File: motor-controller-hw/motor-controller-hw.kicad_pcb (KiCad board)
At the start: 4 copper layers, 162 parts, among them J101 CAN, J102 Throttle, J103 Motor Temp, J104 Transistor Temp, J105 USB_B_Micro, J106 Extra IO, J107 Hall Sensors, J108 CAN_DBG, J109 ABN Encoder, J110 SPI_DBG, J111 Trinamic-Bridge, J301 SWD, J302 User USART, J401 Trinamic_TRMI, J402 TMC4671 USART, Q101 Q_PMOS_GDS, SW301 Reset, SW302 Boot, SW303 User_SW, U101 AP7361C-33, U102 D36V6F5, U201 MCP6004, U202 MCP6004, U203 MCP6004, U204 74HC7014, U205 74HC7014, U206 mcp2562, U301 STM32F303RETx, U401 TMC4671, X401 IQXO-50, Y301 8Mhz

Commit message: Moved chaged order of op-amps to make PCB layout easier. More pcb part positioning
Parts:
- C101, C102, C104, C105, C202, C203, C204, C205, C301, C302, C303, C304, C305, C306, C307, C308, C309, C310, C311, C401, C403, C404, C406, C408, C409, C410, C411, R201, R202, R203, R206, R207, R208, R209, R213, R214, R215, R301, R303, R304, U201, U202: moved to B.Cu
- TP401, TP402: footprint Connector_PinHeader_2.54mm:PinHeader_1x03_P2.54mm_Vertical -> Pin_Headers:Pin_Header_Straight_1x01_Pitch2.54mm
- moved C420 307.0 mm to (88.3, 59.9), turned to 270 degrees
- moved R409 307.0 mm to (88.3, 56.1), turned to 90 degrees
- moved C402 305.8 mm to (87.6, 41.3), turned to 270 degrees
- moved R408 303.4 mm to (87.2, 69.1), turned to 270 degrees
- moved R401 302.8 mm to (87.6, 37.5), turned to 270 degrees
- moved R403 301.9 mm to (92.3, 37.3), turned to 270 degrees
- moved C419 301.2 mm to (89.3, 69.1), turned to 270 degrees
- moved R402 298.0 mm to (85.6, 41.3), turned to 270 degrees
- moved R404 296.8 mm to (92.3, 41.1), turned to 270 degrees
- moved R410 293.8 mm to (89.3, 65.3), turned to 270 degrees
- moved C407 293.5 mm to (90.3, 41.1), turned to 270 degrees
- moved R406 293.3 mm to (95.0, 56.1), turned to 270 degrees
- moved C417 292.6 mm to (95.0, 59.9), turned to 270 degrees
- moved C418 289.4 mm to (100.8, 60.1), turned to 270 degrees
- moved R407 283.8 mm to (100.8, 56.1), turned to 270 degrees
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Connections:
- J110 pad 3: /TMC4671/SPI_MOSI -> /TMC4671/SPI_MISO
- J110 pad 4: /TMC4671/SPI_MISO -> /TMC4671/SPI_MOSI
- U201 pad 1: Net-(R201-Pad2) -> /A_Out2
- U201 pad 10: /IO Protection/A_Out1 -> /Throttle
- U201 pad 12: /IO Protection/A_Out2 -> Net-(C203-Pad1)
- U201 pad 13: /A_Out2 -> /IO Protection/Throttle
- U201 pad 14: /A_Out2 -> /IO Protection/Throttle
- U201 pad 2: Net-(R201-Pad2) -> /A_Out2
- U201 pad 3: /Throttle -> /IO Protection/A_Out2
- U201 pad 5: Net-(C203-Pad1) -> /IO Protection/A_Out1
- U201 pad 6: /IO Protection/Throttle -> /A_Out1
- U201 pad 7: /IO Protection/Throttle -> /A_Out1
- U201 pad 8: /A_Out1 -> Net-(R201-Pad2)
- U201 pad 9: /A_Out1 -> Net-(R201-Pad2)

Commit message: Working PCB Layout
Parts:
- C212, C215, C216, C217, C218, C219, C220, D101, R102, R210, R211, R212, R216, R217, R218, R219, R220, R408, U205: moved to B.Cu
- R207, R208, R209, R213, R214, R215: moved to F.Cu
- moved R408 179.0 mm to (265.9, 57.9), turned to 0 degrees
- moved R409 178.1 mm to (265.9, 68.1), turned to 180 degrees
- moved C420 177.8 mm to (265.9, 66.0), turned to 0 degrees
- moved C419 177.0 mm to (265.9, 57.9), turned to 0 degrees
- moved R410 176.7 mm to (265.9, 59.9), turned to 180 degrees
- moved R406 171.1 mm to (265.9, 64.0), turned to 180 degrees
- moved C417 171.0 mm to (265.9, 62.0), turned to 0 degrees
- moved R407 165.9 mm to (265.9, 72.1), turned to 180 degrees
- moved C418 165.4 mm to (265.9, 70.1), turned to 0 degrees
- moved R403 161.2 mm to (249.8, 71.6)
- moved R404 161.2 mm to (249.8, 75.4)
- moved C407 161.2 mm to (247.8, 75.4)
- moved C402 160.1 mm to (244.0, 75.5)
- moved R401 160.1 mm to (244.0, 71.7)
- moved R402 160.1 mm to (242.0, 75.5)
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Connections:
- C420 pad 1: /Batt_Current -> /TMC4671/Batt_I
- D301 pad 1: Net-(D301-Pad1) -> GNDD
- D301 pad 2: /STM32/CAN_Status -> Net-(D301-Pad2)
- D302 pad 1: Net-(D302-Pad1) -> GNDD
- D302 pad 2: /STM32/Heartbeat -> Net-(D302-Pad2)
- D303 pad 1: Net-(D303-Pad1) -> GNDD
- D303 pad 2: /STM32/User_LED -> Net-(D303-Pad2)
- R305 pad 1: GNDD -> Net-(D301-Pad2)
- R305 pad 2: Net-(D301-Pad1) -> /STM32/CAN_Status
- R306 pad 1: GNDD -> Net-(D302-Pad2)
- R306 pad 2: Net-(D302-Pad1) -> /STM32/Heartbeat
- R307 pad 1: GNDD -> Net-(D303-Pad2)
- R307 pad 2: Net-(D303-Pad1) -> /STM32/User_LED
- R409 pad 2: /Batt_Current -> /TMC4671/Batt_I
- TP422 pad 2: /Batt_Current -> /TMC4671/Batt_I
- U401 pad 21: /Batt_Current -> /TMC4671/Batt_I

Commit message: Started routing
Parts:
- moved J402 0.19 mm to (227.3, 68.3)
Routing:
- net GNDD: track 0.00 -> 6.33 mm, vias 0 -> 1
- net /Throttle: track 0.00 -> 6.32 mm, vias 0 -> 1
- net Net-(R202-Pad2): track 0.00 -> 5.65 mm
- net Net-(C203-Pad1): track 0.00 -> 4.48 mm
- net Net-(C205-Pad1): track 0.00 -> 4.29 mm
- net Net-(C204-Pad1): track 0.00 -> 4.13 mm
- net Net-(R201-Pad2): track 0.00 -> 3.80 mm
- net Net-(R203-Pad2): track 0.00 -> 3.68 mm
- net /IO Protection/Throttle: track 0.00 -> 1.27 mm
- net /A_Out1: track 0.00 -> 1.27 mm
- net /A_Out2: track 0.00 -> 1.27 mm
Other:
- net class Default: clearance 0.2 -> 0.1778; trace_width 0.25 -> 0.3048; via_dia 0.8 -> 0.762; via_drill 0.4 -> 0.381
- net class analog_signal added: clearance 0.1778, trace_width 0.3048, via_dia 0.762, via_drill 0.381
- net class power added: clearance 0.254, trace_width 0.508, via_dia 1.4224, via_drill 1.016
- net class serial_signal added: clearance 0.1778, trace_width 0.2032, via_dia 0.762, via_drill 0.381
- net class small_signal added: clearance 0.1778, trace_width 0.2032, via_dia 0.762, via_drill 0.381
- rule trace_clearance: 0.2 -> 0.1778
- rule trace_min: 0.2 -> 0.1524
- rule via_min_drill: 0.3 -> 0.254
- rule via_min_size: 0.4 -> 0.508

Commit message: PCB Routing
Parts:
- moved C213 159.2 mm to (31.4, 69.7)
- moved C214 159.2 mm to (31.3, 66.2)
- moved C415 159.2 mm to (33.5, 60.3)
- moved C416 159.2 mm to (30.1, 60.1)
- moved C210 148.1 mm to (100.3, 113.0), turned to 90 degrees
- moved C216 147.5 mm to (111.1, 121.3)
- moved C219 147.5 mm to (94.9, 121.6)
- moved C402 147.5 mm to (101.4, 113.0)
- moved J109 147.5 mm to (99.3, 129.6)
- moved R208 147.5 mm to (111.1, 121.3)
- moved R211 147.5 mm to (111.1, 116.7)
- moved R214 147.5 mm to (94.9, 121.6)
- moved R218 147.5 mm to (94.9, 117.0)
- moved R401 147.5 mm to (101.4, 109.2)
- moved C215 147.5 mm to (109.1, 121.3)
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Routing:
- net +5V: track 0.00 -> 322.6 mm, vias 0 -> 12
- net GNDD: track 6.33 -> 285.8 mm, vias 1 -> 45
- net +3V3: track 0.00 -> 99.8 mm, vias 0 -> 27
- net /MotorTemp: track 0.00 -> 95.7 mm, vias 0 -> 1
- net +BATT: track 0.00 -> 78.8 mm, vias 0 -> 2
- net /SPI_SS: track 0.00 -> 77.5 mm, vias 0 -> 2
- net /Vin: track 0.00 -> 73.3 mm, vias 0 -> 1
- net /SPI_MISO: track 0.00 -> 70.5 mm, vias 0 -> 2
- net /TMC4671/1v8: track 0.00 -> 70.3 mm, vias 0 -> 8
- net /SPI_MOSI: track 0.00 -> 68.3 mm, vias 0 -> 2
- net /SPI_SCK: track 0.00 -> 64.4 mm, vias 0 -> 2
- net /A_Out1: track 1.27 -> 61.8 mm, vias 0 -> 1
- net /A_Out2: track 1.27 -> 58.8 mm, vias 0 -> 1
- net /TMC4671/En_In: track 0.00 -> 47.9 mm, vias 0 -> 2
- net /TMC4671/B_Current: track 0.00 -> 42.5 mm, vias 0 -> 1
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- added copper zone on In2.Cu, net +3V3
- added copper zone on In1.Cu, net GNDD
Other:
- net class serial_signal: trace_width 0.2032 -> 0.254

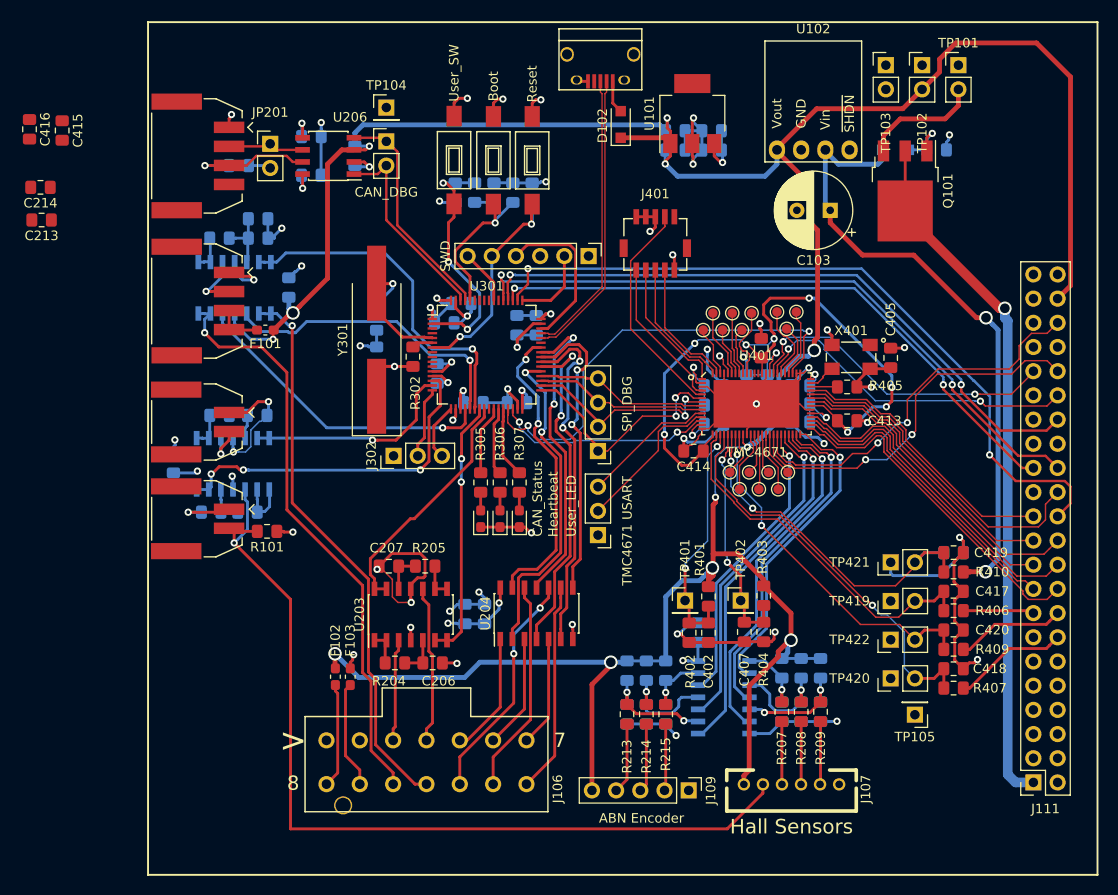
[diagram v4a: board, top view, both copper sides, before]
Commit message: Added mounting holes to pcb
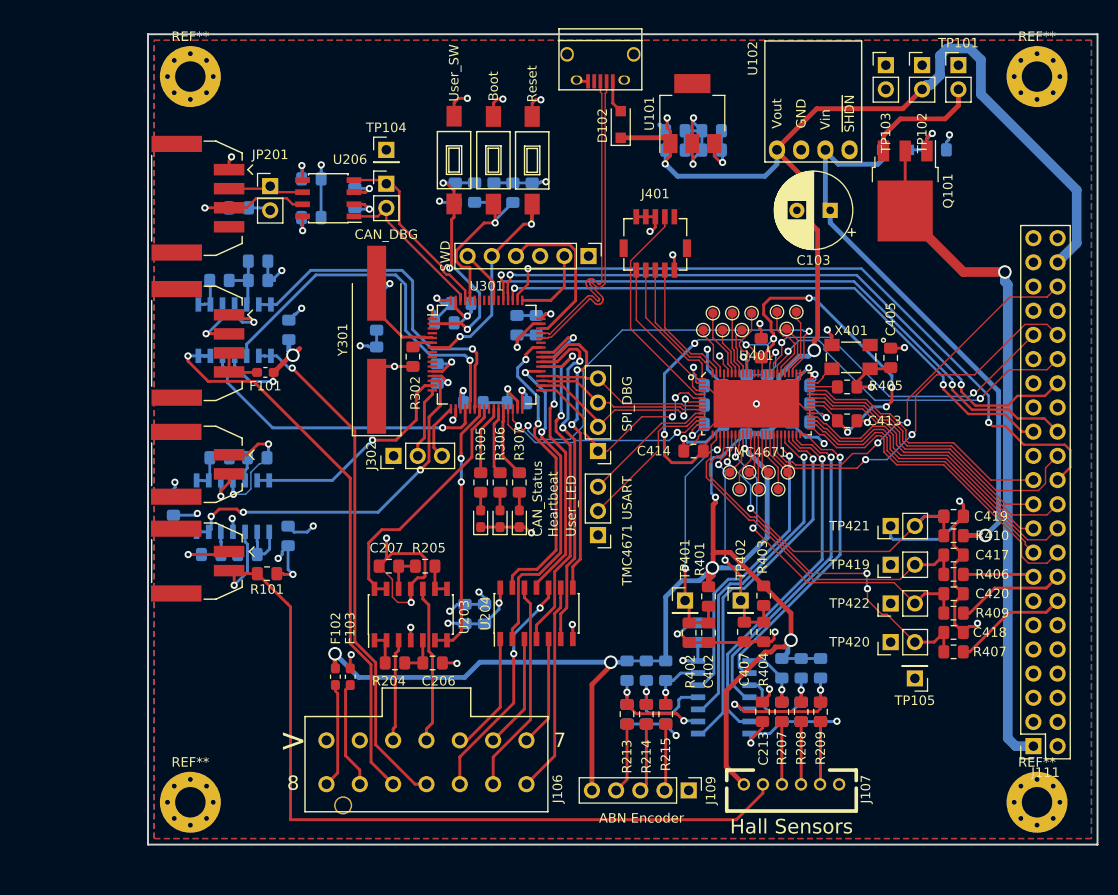
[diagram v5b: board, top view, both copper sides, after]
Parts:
- added REF**: MountingHole_3.2mm_M3_Pad_Via, Mounting_Holes:MountingHole_3.2mm_M3_Pad_Via, F.Cu at (135.9, 130.8)
- added REF**: MountingHole_3.2mm_M3_Pad_Via, Mounting_Holes:MountingHole_3.2mm_M3_Pad_Via, F.Cu at (47.0, 54.6)
- added REF**: MountingHole_3.2mm_M3_Pad_Via, Mounting_Holes:MountingHole_3.2mm_M3_Pad_Via, F.Cu at (47.0, 130.8)
- added REF**: MountingHole_3.2mm_M3_Pad_Via, Mounting_Holes:MountingHole_3.2mm_M3_Pad_Via, F.Cu at (135.9, 54.6)
- C214, C415, C416: moved to B.Cu
- moved C213 91.6 mm to (107.1, 121.3), turned to 270 degrees
- moved C416 83.4 mm to (107.5, 91.1), turned to 90 degrees
- moved C415 78.1 mm to (105.3, 91.1), turned to 90 degrees
- moved C214 44.9 mm to (57.3, 102.8), turned to 90 degrees
- moved C201 4.45 mm to (57.3, 81.2)
- moved C203 4.45 mm to (54.1, 74.0)
- moved C204 4.45 mm to (49.2, 104.8)
- moved C212 4.45 mm to (59.7, 65.4)
- moved JP201 4.45 mm to (55.4, 66.1)
- moved R101 4.45 mm to (55.0, 106.8)
- moved R202 4.45 mm to (53.0, 104.8)
- moved U201 4.45 mm to (51.6, 81.2)
- moved U202 4.45 mm to (51.5, 99.7)
- moved C202 4.45 mm to (64.3, 67.4)
- moved J101 4.45 mm to (42.9, 67.4)
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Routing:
- net GNDD: track 285.8 -> 351.4 mm, vias 45 -> 47
- net +5V: track 322.6 -> 283.2 mm
- net +BATT: track 78.8 -> 71.3 mm, vias 2 -> 1
- net /IO Protection/A_Out2: track 31.9 -> 39.4 mm
- net +3V3: track 99.8 -> 106.4 mm, vias 27 -> 29
- net /MotorTemp: track 95.7 -> 90.1 mm
- net /A_Out2: track 58.8 -> 54.3 mm
- net /IO Protection/CAN_Rx: track 23.7 -> 19.8 mm
- net Net-(C217-Pad1): track 11.8 -> 15.7 mm
- net /IO Protection/CAN_Tx: track 21.1 -> 17.3 mm
- net /USB_D-: track 30.7 -> 34.3 mm
- net /SPI_SS: track 77.5 -> 74.0 mm
- net /USB_D+: track 30.2 -> 33.7 mm
- net /IO Protection/TransistorTemp: track 22.4 -> 24.4 mm
- net /IO Protection/MotorTemp: track 36.4 -> 38.3 mm
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- added copper zone on B.Cu, net +5V
- added copper zone on F.Cu, net +5V
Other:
- board outline added: 99.7 x 85.1 mm
- net class power: clearance 0.254 -> 0.1778
- rule trace_min: 0.1524 -> 0.127

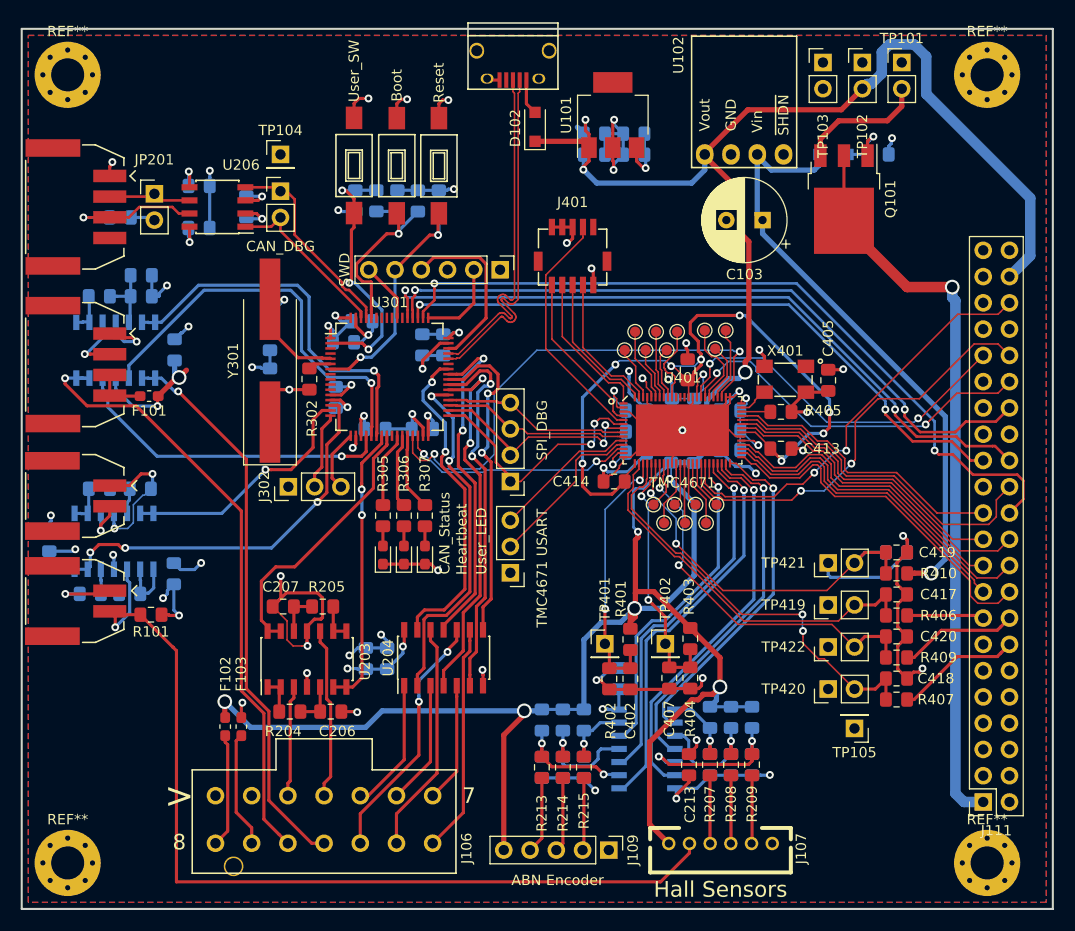
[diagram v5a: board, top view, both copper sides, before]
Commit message: Adding BOM, changed some footprints -Changed footprints to linux models in schematics -Added field Digi-key# to all components -Started filling in said field
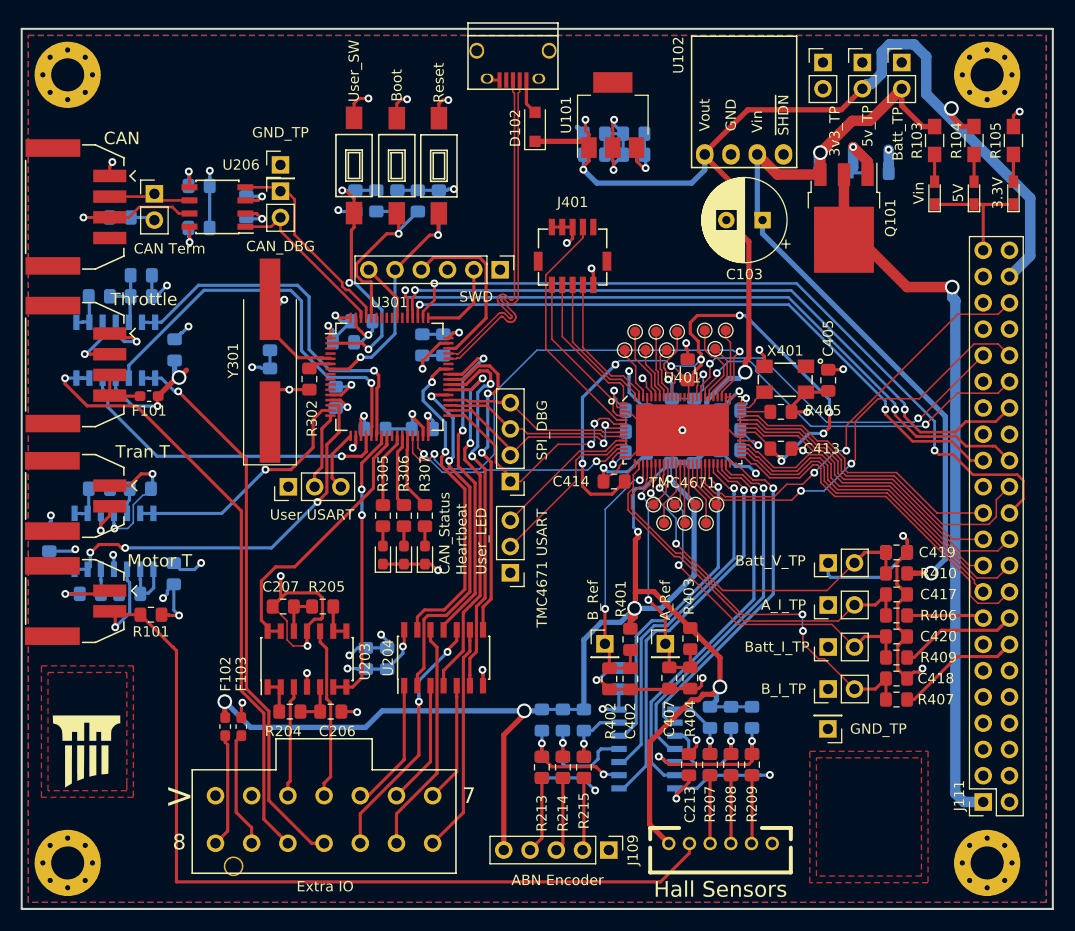
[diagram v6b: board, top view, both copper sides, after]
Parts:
- added D103: Vin, LEDs:LED_0603_HandSoldering, F.Cu at (130.8, 66.0)
- added D104: 5V, LEDs:LED_0603_HandSoldering, F.Cu at (134.6, 66.0)
- added D105: 3.3V, LEDs:LED_0603_HandSoldering, F.Cu at (138.4, 66.0)
- added G***: LOGO, supermileage_footprints:cedarville-logo, F.Cu at (49.0, 118.6)
- added G***: LOGO, supermileage_footprints:shell-logo, F.Cu at (24.6, 145.8)
- added G***: LOGO, supermileage_footprints:shell-logo, F.Cu at (124.5, 126.4)
- added R103: 10K, Resistors_SMD:R_0805_HandSoldering, F.Cu at (130.8, 61.0)
- added R104: 1K, Resistors_SMD:R_0805_HandSoldering, F.Cu at (134.6, 61.0)
- added R105: 510R, Resistors_SMD:R_0805_HandSoldering, F.Cu at (138.4, 61.0)
- C215, C216, C217, C218, C219, C220: value 100n -> 100p
- C417, C418, C420: value 100n -> 10n
- J103: value Motor Temp -> Motor T
- J104: value Transistor Temp -> Tran T
- JP201: value CAN Termination -> CAN Term
- TP101: value 5v_TP -> Batt_TP
- moved TP105 2.57 mm to (120.5, 117.9)
- moved Q101 1.83 mm to (122.0, 68.5)
- moved D101 1.78 mm to (121.0, 64.1)
- moved R102 1.78 mm to (125.3, 64.1)
- moved TP104 1.02 mm to (67.6, 63.3)
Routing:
- net GNDD: track 351.4 -> 364.8 mm
- net +BATT: track 71.3 -> 78.0 mm, vias 1 -> 2
- net +5V: track 283.2 -> 287.7 mm, vias 12 -> 13
- net Net-(D105-Pad2): track 0.00 -> 2.63 mm
- net Net-(D104-Pad2): track 0.00 -> 2.63 mm
- net Net-(D103-Pad2): track 0.00 -> 2.63 mm
- net +3V3: track 106.4 -> 108.2 mm, vias 29 -> 30
- net Net-(D101-Pad2): track 6.01 -> 7.83 mm
- added copper zone on F.Cu, net (none)
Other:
- board text added: "CAN 1. >GND 2. CANL 3. CANH 4. N/C"
- board text added: "Cedarville University Samuel Ellicott: Fall 2018"
- board text added: "Extra IO 1. GND | 8. 5v 2. GND | 9. 3.3v 3. Ain1 | 10. Aout1 4. Ain2 | 11. Aout 2 5. Din1 | 12. Dout 1 6. Din2 | 13. Dout 2 7. Din3 | 14. Din 4"
- board text added: "High Efficiency Motor Controller Control PCB - v1.0"
- board text added: "Motor Temp 1. >GND 2. Temp in"
- board text added: "Throttle 1. >GND 2. Throttle 3. 5v 4. 5v"
- board text added: "Transistor Temp 1. >GND 2. Temp in"

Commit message: Moved some parts into the project parts library messed with the PCB slightly
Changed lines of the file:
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@@
-(kicad_pcb (version 20171130) (host pcbnew "(5.0.0-rc2-dev-670-ga3770bf6e)")
+(kicad_pcb (version 20171130) (host pcbnew 5.0.1)
   (general
     (thickness 1.6)
@@
     (pad_drill 3.2)
     (pad_to_mask_clearance 0.2)
+    (solder_mask_min_width 0.25)
     (aux_axis_origin 0 0)
     (visible_elements 7FFFFF7F)
@@
       (hpglpennumber 1)
       (hpglpenspeed 20)
-      (hpglpendiameter 15)
+      (hpglpendiameter 15.000000)
       (psnegative false)
       (psa4output false)
@@
     (tags "capacitor handsolder")
     (attr smd)
-    (fp_text reference C401 (at -3.8862 0.635 270) (layer B.SilkS)
+    (fp_text reference C401 (at -3.7084 0.5588 90) (layer B.SilkS)
       (effects (font (size 1 1) (thickness 0.15)) (justify mirror))
     )
@@
     (tags "capacitor handsolder")
     (attr smd)
-    (fp_text reference C412 (at 0 -1.65 90) (layer F.SilkS) hide
+    (fp_text reference C412 (at 0.3048 -3.7338 180) (layer F.SilkS)
       (effects (font (size 1 1) (thickness 0.15)))
     )
@@
     (clearance 0.075)
     (attr smd)
-    (fp_text reference U401 (at 0 -5.08) (layer F.SilkS)
-      (effects (font (size 1 1) (thickness 0.05)))
+    (fp_text reference U401 (at -9.271 -2.159) (layer F.SilkS)
+      (effects (font (size 1.016 1.016) (thickness 0.14478)))
     )
-    (fp_text value TMC4671 (at 0 5.08) (layer F.SilkS)
+    (fp_text value TMC4671 (at 0 5.08) (layer F.Fab)
       (effects (font (size 1 1) (thickness 0.05)))
     )
